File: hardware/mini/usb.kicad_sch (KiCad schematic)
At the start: 3 parts, among them J1 USB_C_Receptacle_USB2.0_16P, J2 USB_C_Receptacle_USB2.0_16P, U4 CH224K

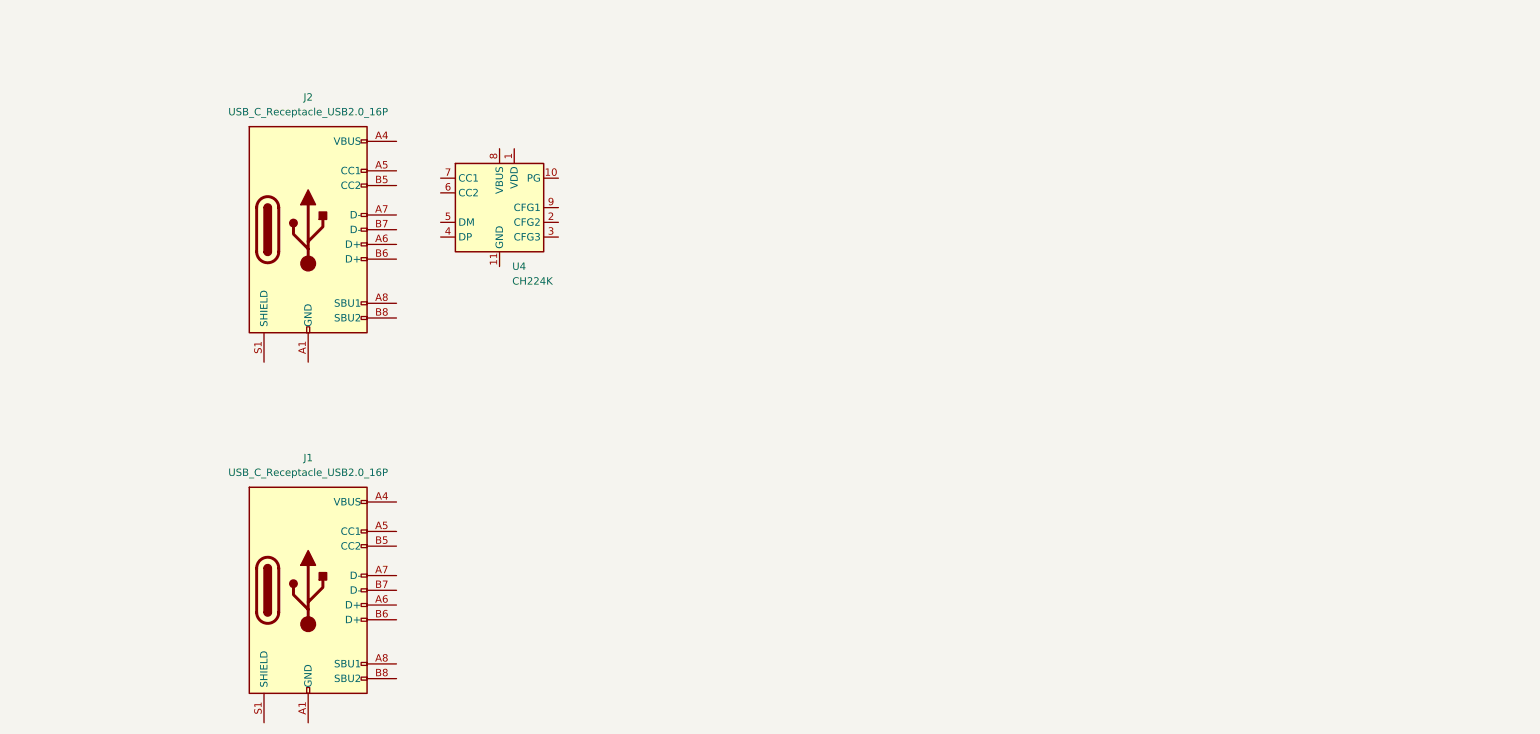
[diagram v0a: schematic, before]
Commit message: finalize parts in schematic
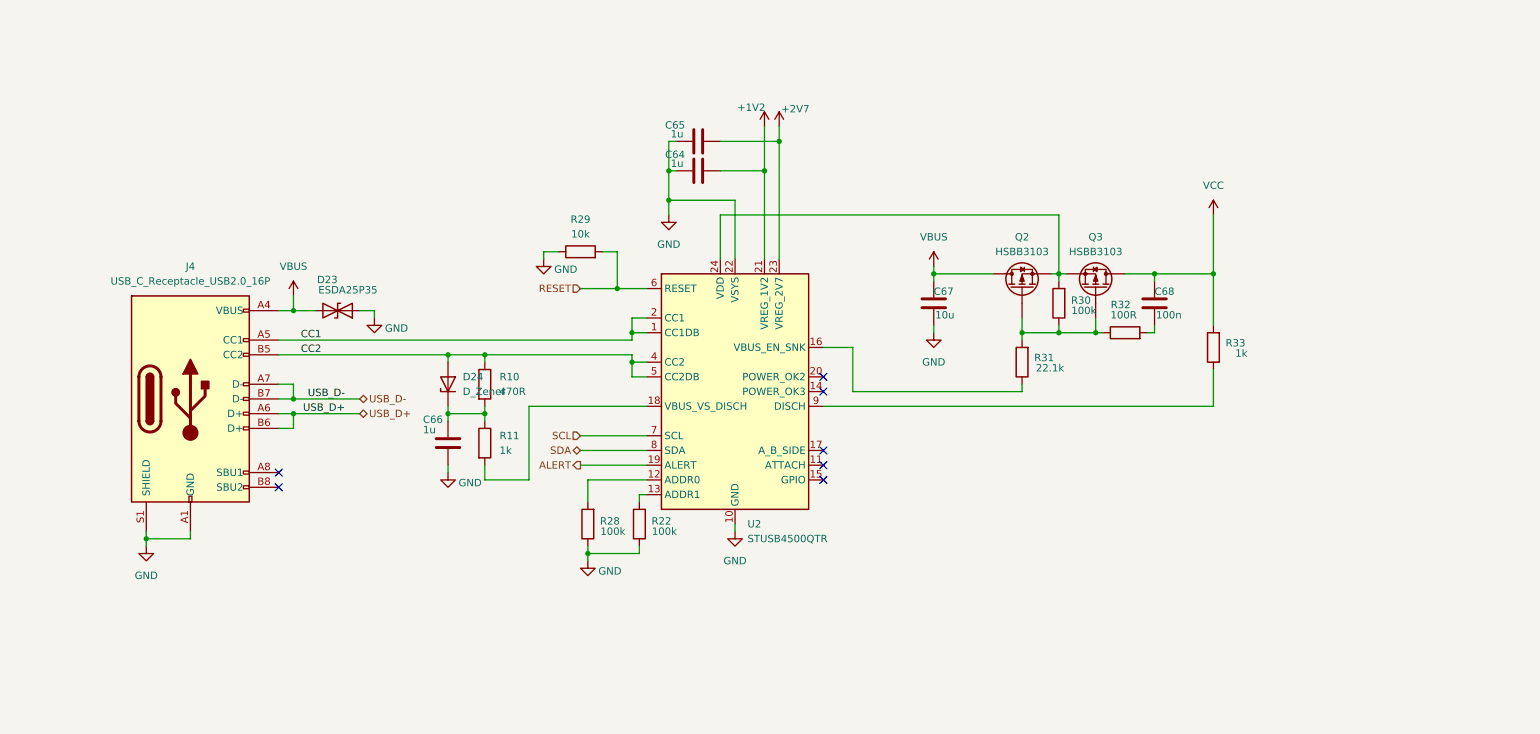
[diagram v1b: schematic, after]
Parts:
- removed J1, J2: USB_C_Receptacle_USB2.0_16P, symbol Connector:USB_C_Receptacle_USB2.0_16P
- removed U4: CH224K, Package_SO:SSOP-10-1EP_3.9x4.9mm_P1mm_EP2.1x3.3mm, symbol Interface_USB:CH224K
- added C64, C65, C66: 1u, Capacitor_SMD:C_1206_3216Metric, symbol Device:C
- added C67: 10u, Capacitor_SMD:C_1206_3216Metric, symbol Device:C
- added C68: 100n, Capacitor_SMD:C_0402_1005Metric, symbol Device:C
- added D23: ESDA25P35, symbol Device:D_TVS
- added D24: D_Zener, symbol Device:D_Zener
- added J4: USB_C_Receptacle_USB2.0_16P, symbol Connector:USB_C_Receptacle_USB2.0_16P
- added Q2, Q3: HSBB3103, symbol Device:Q_PMOS
- added R10: 470R, symbol Device:R
- added R11, R33: 1k, symbol Device:R
- added R22, R28, R30: 100k, symbol Device:R
- added R29: 10k, symbol Device:R
- added R31: 22.1k, symbol Device:R
- added R32: 100R, Resistor_SMD:R_0402_1005Metric, symbol Device:R
- added U2: STUSB4500QTR, Package_DFN_QFN:QFN-24-1EP_4x4mm_P0.5mm_EP2.7x2.7mm, symbol Interface_USB:STUSB4500QTR
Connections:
- new net: C66.1, D24.1 (K), R10.2, R11.1
- new net: Q2.G, Q3.G, R30.1, R31.2, R32.1
- new net: Q2.S, Q3.S, R30.2, U2.24 (VDD)
- new net: C68.2, R32.2
- new net: R28.2, U2.12 (ADDR0)
- new net: R22.2, U2.13 (ADDR1)
- new net: R31.1, U2.16 (VBUS_EN_SNK)
- new net: R11.2, U2.18 (VBUS_VS_DISCH)
- new net: R33.1, U2.9 (DISCH)
- new net +1V2: C64.1, U2.21 (VREG_1V2)
- new net +2V7: C65.1, U2.23 (VREG_2V7)
- new net ALERT: U2.19 (ALERT)
- new net CC1: J4.A5 (CC1), U2.1 (CC1DB), U2.2 (CC1)
- new net CC2: D24.2 (A), J4.B5 (CC2), R10.1, U2.4 (CC2), U2.5 (CC2DB)
- new net GND: C64.2, C65.2, C66.2, C67.2, D23.1 (A1), J4.A1 (GND), J4.A12 (GND), J4.B1 (GND), J4.B12 (GND), J4.S1 (SHIELD), R22.1, R28.1, R29.1, U2.10 (GND), U2.22 (VSYS), U2.25 (GND)
- new net RESET: R29.2, U2.6 (RESET)
- new net SCL: U2.7 (SCL)
- new net SDA: U2.8 (SDA)
- new net USB_D+: J4.A6 (D+), J4.B6 (D+)
- new net USB_D-: J4.A7 (D-), J4.B7 (D-)
- new net VBUS: C67.1, D23.2 (A2), J4.A4 (VBUS), J4.A9 (VBUS), J4.B4 (VBUS), J4.B9 (VBUS), Q2.D
- new net VCC: C68.1, Q3.D, R33.2
- no-connect marks 0 -> 7

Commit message: route most
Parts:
- added NT1: NetTie_2, symbol Device:NetTie_2
- renumbered C66 to C72, C65 to C73, C64 to C74, C67 to C75, C68 to C76, D23 to D1, D24 to D2, J4 to J1, Q2 to Q1, Q3 to Q2, R10 to R33, R11 to R34, R29 to R35, R28 to R36, R22 to R37, R31 to R38, R30 to R39, R32 to R40, R33 to R41, U2 to U11
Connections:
- net GND: now also NT1.2; no longer C75.2, D1.1 (A1), J1.A1 (GND), J1.A12 (GND), J1.B1 (GND), J1.B12 (GND), J1.S1 (SHIELD)
- new net GNDPWR: C75.2, D1.1 (A1), J1.A1 (GND), J1.A12 (GND), J1.B1 (GND), J1.B12 (GND), J1.S1 (SHIELD), NT1.1
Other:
- note added: "Place next to STUB4500 Transfer of power domain into GND from GNDPWR"

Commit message: ERC run
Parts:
- renumbered C72 to C82, C73 to C83, C74 to C84, C75 to C85, C76 to C86, D1 to D23, D2 to D24, J1 to J5, Q1 to Q2, Q2 to Q3, R33 to R41, R34 to R42, R35 to R43, R36 to R44, R37 to R45, R38 to R46, R39 to R47, R40 to R48, R41 to R49, U11 to U10
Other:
- moved on the sheet: C83, C84, D23

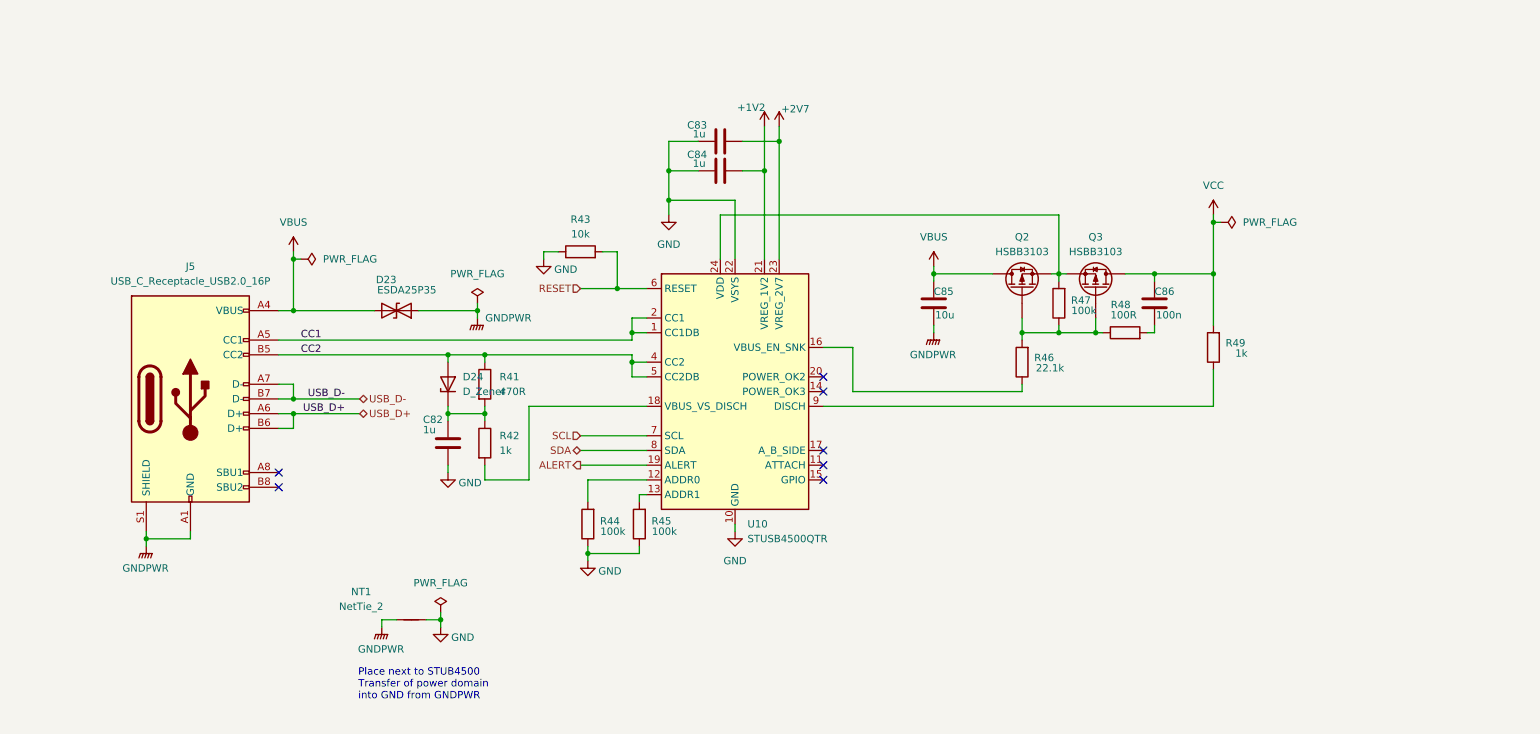
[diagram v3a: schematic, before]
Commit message: assign footprints & LCSC id
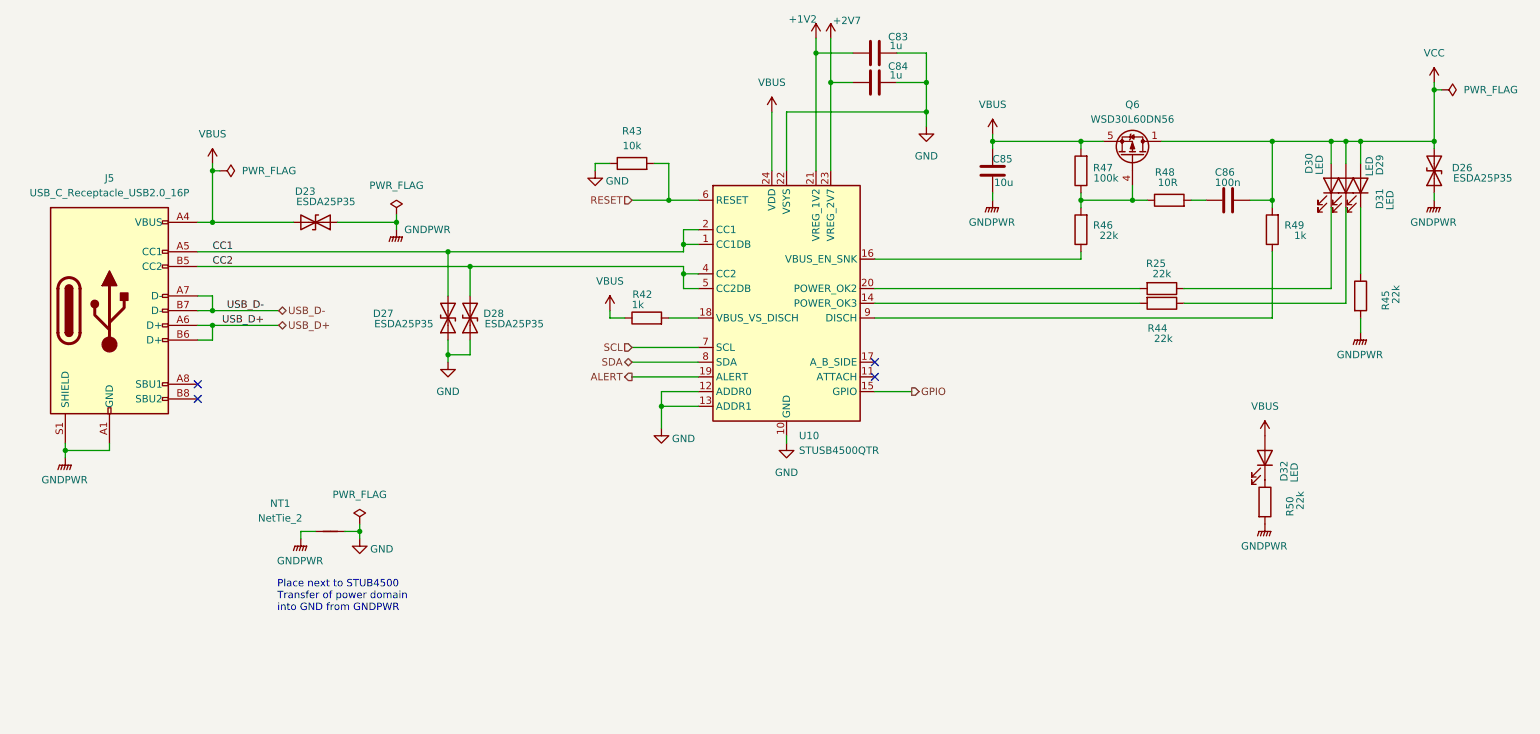
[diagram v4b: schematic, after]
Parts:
- removed C82: 1u, Capacitor_SMD:C_1206_3216Metric, symbol Device:C
- removed D24: D_Zener, symbol Device:D_Zener
- removed Q2, Q3: HSBB3103, symbol Device:Q_PMOS
- removed R41: 470R, symbol Device:R
- added D26, D27, D28: ESDA25P35, symbol Device:D_TVS
- added D29, D30, D31, D32: LED, LED_SMD:LED_0603_1608Metric, symbol Device:LED
- added Q6: WSD30L60DN56, Package_DFN_QFN:PQFN-8-EP_6x5mm_P1.27mm_Generic, symbol Transistor_FET:CSD25402Q3A
- added R25, R50: 22k, Resistor_SMD:R_0402_1005Metric, symbol Device:R
- D23: LCSC (none) -> C1974707
- J5: footprint (none) -> Connector_USB:USB_C_Receptacle_GCT_USB4105-xx-A_16P_TopMnt_Horizontal; LCSC (none) -> C165948
- R42, R49: footprint (none) -> Resistor_SMD:R_0402_1005Metric; LCSC (none) -> C11702
- R43: footprint (none) -> Resistor_SMD:R_0402_1005Metric; LCSC (none) -> C25905
- R44, R45: value 100k -> 22k; footprint (none) -> Resistor_SMD:R_0402_1005Metric; LCSC (none) -> C25768
- R46: value 22.1k -> 22k; footprint (none) -> Resistor_SMD:R_0402_1005Metric; LCSC (none) -> C25768
- R47: footprint (none) -> Resistor_SMD:R_0402_1005Metric; LCSC (none) -> C25741
- R48: value 100R -> 10R; LCSC C25076 -> C25077
- U10: LCSC (none) -> C2678061
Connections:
- net +1V2: now also C83.1; no longer C84.1
- net +2V7: now also C84.1; no longer C83.1
- net CC1: now also D27.2 (A2)
- net CC2: now also D28.2 (A2)
- net GND: now also U10.12 (ADDR0), U10.13 (ADDR1), D27.1 (A1), D28.1 (A1); no longer R44.1, R45.1
- net GNDPWR: now also R45.2, D26.1 (A1), R50.2
- net VBUS: now also R42.1, R47.2, U10.24 (VDD), D32.2 (A), Q6.5 (S)
- net VCC: now also D26.2 (A2), D29.2 (A), D30.2 (A), D31.2 (A), Q6.1 (D), Q6.2 (D), Q6.3 (D)
- net at R46.2, R47.1, R48.1: now also Q6.4 (G)
- net at R44.2: now also U10.14 (POWER_OK3); no longer U10.12 (ADDR0)
- net GPIO: now reaches U10.15 (GPIO)
- net at U10.20 (POWER_OK2): now also R25.2
- new net: D30.1 (K), R44.1
- new net: D31.1 (K), R45.1
- new net: D29.1 (K), R25.1
- new net: D32.1 (K), R50.1
- no-connect marks 7 -> 4
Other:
- moved on the sheet: C83, C84, C85, C86, D23, J5, NT1, R42, R43, R46, R47, R48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

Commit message: build all footprints
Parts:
- removed D23, D26, D27, D28: ESDA25P35, symbol Device:D_TVS
- added D23, D26, D27, D33: ESDA25P35, protovolt_mini_fp:D_1610_4027Metric, symbol Device:D_Zener
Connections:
- net CC1: now also D26.1 (K)
- net CC2: now also D27.1 (K)
- net GND: now also D26.2 (A), D27.2 (A)
- net GNDPWR: now also D23.2 (A), D33.2 (A)
- net VBUS: now also D33.1 (K)
- net VCC: now also D23.1 (K)

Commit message: import to PCB
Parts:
- NT1: footprint (none) -> NetTie:NetTie-2_SMD_Pad0.5mm
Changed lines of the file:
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@@
 			)
 		)
-		(property "Footprint" ""
+		(property "Footprint" "NetTie:NetTie-2_SMD_Pad0.5mm"
 			(at 80.01 133.35 0)
 			(effects

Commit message: route digitals
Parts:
- C83, C84: footprint Capacitor_SMD:C_1206_3216Metric -> Capacitor_SMD:C_0603_1608Metric; LCSC C1848 -> C15849
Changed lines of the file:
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@@
 			)
 		)
-		(property "Footprint" "Capacitor_SMD:C_1206_3216Metric"
+		(property "Footprint" "Capacitor_SMD:C_0603_1608Metric"
 			(at 177.8 54.9148 0)
 			(effects
@@
 			)
 		)
-		(property "LCSC" "C1848"
+		(property "LCSC" "C15849"
 			(at 173.99 55.88 0)
 			(effects
@@
 			)
 		)
-		(property "Footprint" "Capacitor_SMD:C_1206_3216Metric"
+		(property "Footprint" "Capacitor_SMD:C_0603_1608Metric"
 			(at 177.8 49.8348 0)
 			(effects
@@
 			)
 		)
-		(property "LCSC" "C1848"
+		(property "LCSC" "C15849"
 			(at 173.99 50.8 0)
 			(effects
